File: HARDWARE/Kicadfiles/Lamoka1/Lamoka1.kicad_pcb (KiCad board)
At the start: 2 copper layers, 156.4 x 124.8 mm, 136 parts, among them IC1 INA240A2DR, J1 2606-1108/010-000, J2 2606-1352, J3 USB_C_Receptacle_USB2.0_14P, J4 470531000, J5 2604-1103, J6 Male-Header, J7 Male-Header, Q1 25V 60A N-Ch, Q2 30V 56A N-Ch, Q3 100V 150A N-Ch, Q4 100V 150A N-Ch, Q5 100V 150A N-Ch, Q6 100V 150A N-Ch, SW1 B3F-4055, U1 RP2354A, U10 ADS7128IRTER, U2 AMS1117-3.3, U3 74AHCT1G125, U4 LM5122MH/NOPB, U5 UCC27735DR, U6 UCC27735DR, U7 TPS62160DSGR, U8 TMP235A2DBZR, U9 TMP235A2DBZR, X1 ABM8-272-T3

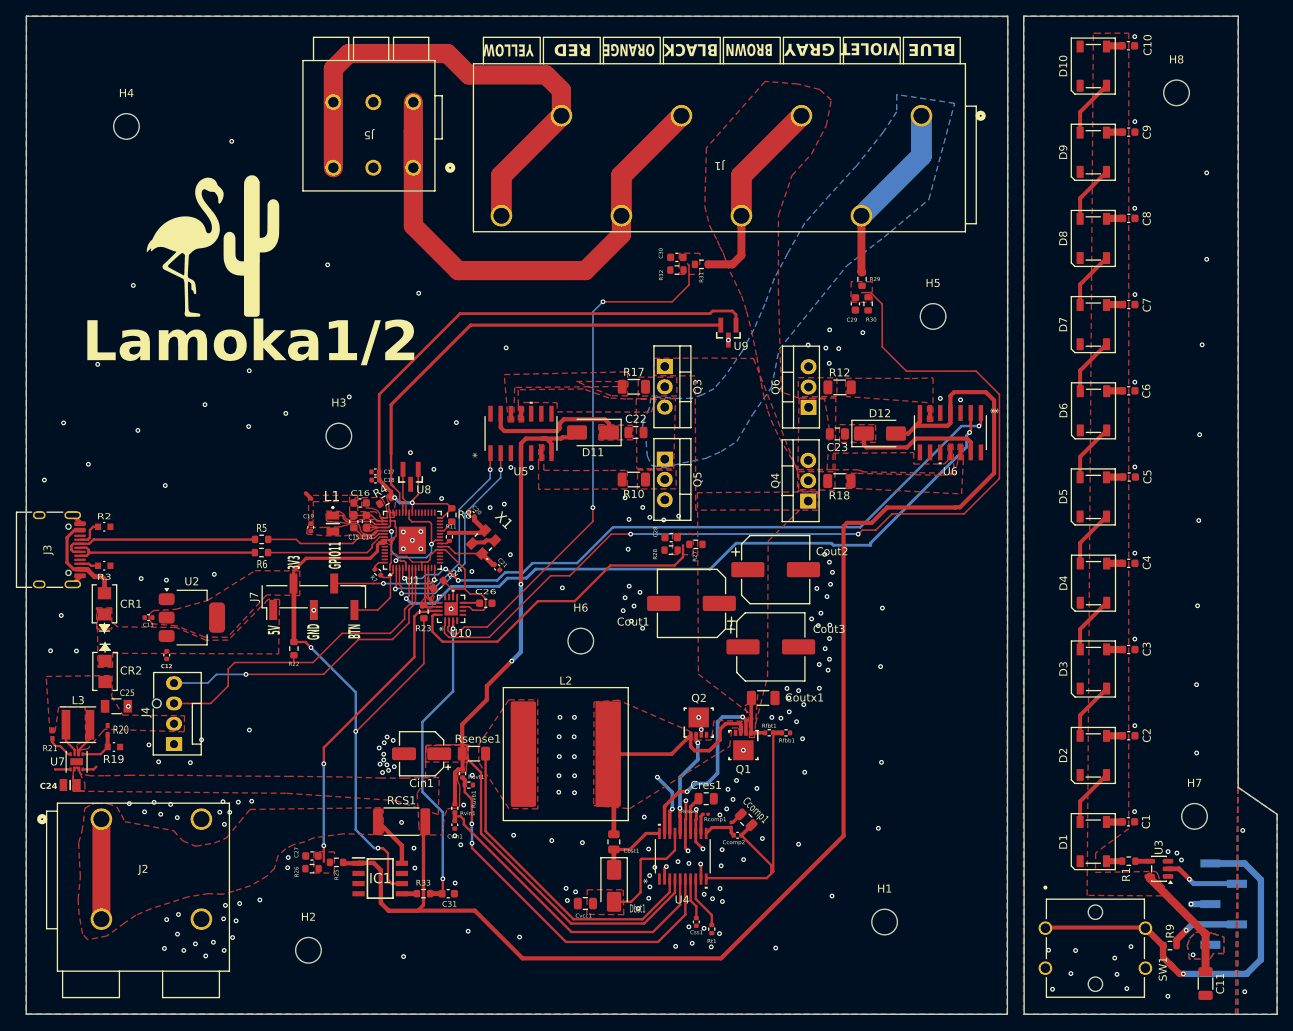
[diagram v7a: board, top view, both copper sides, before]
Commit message: Some more slight improvements, general. ADD picture to main readme, etc
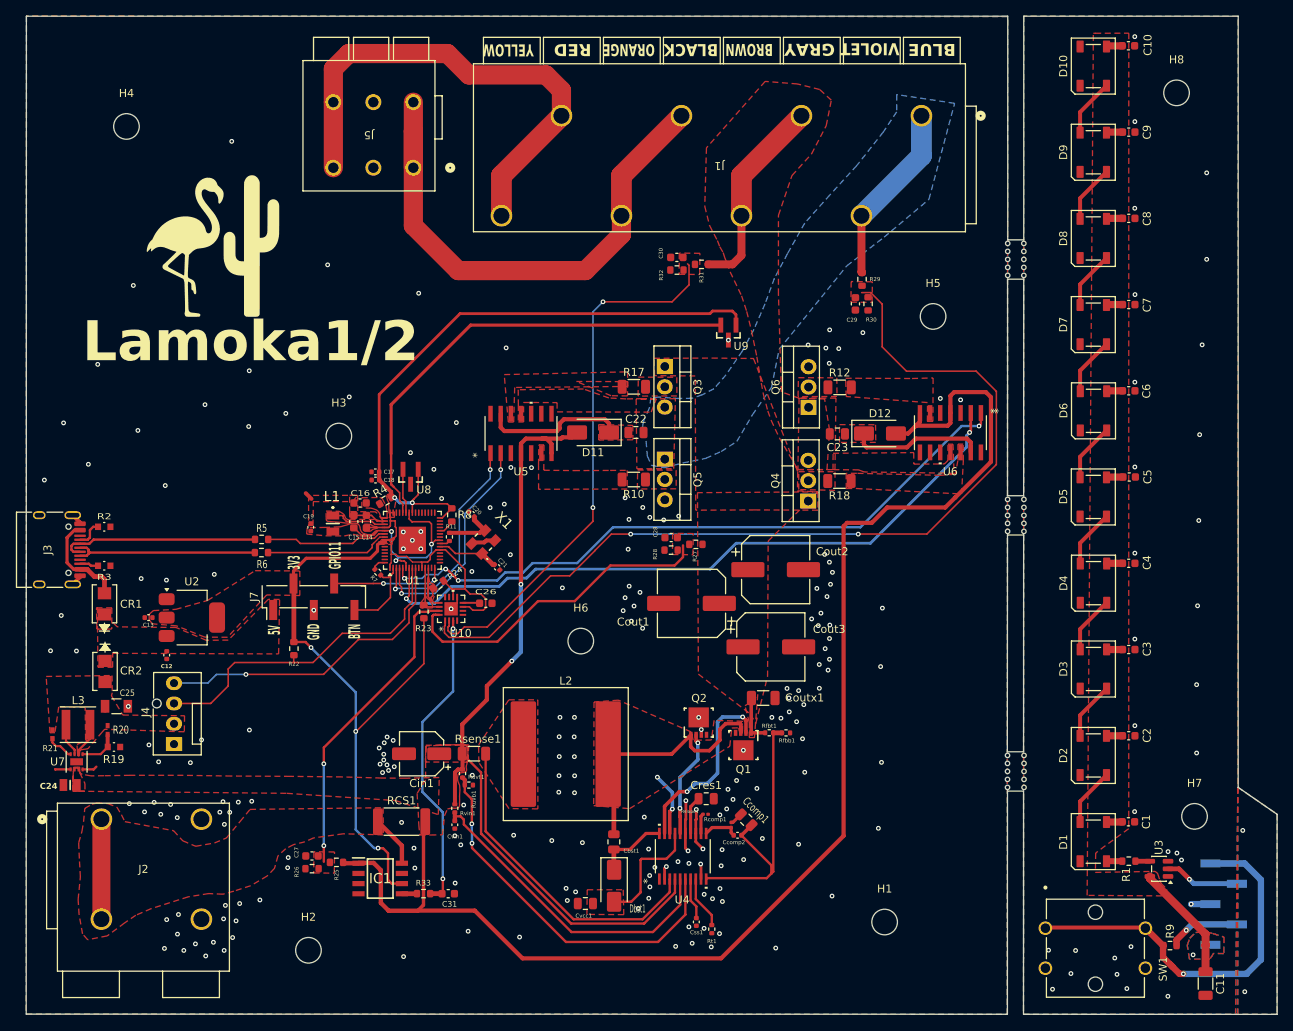
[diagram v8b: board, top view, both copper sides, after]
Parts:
- added MTB1: MouseBite-5x0.55, MouseBite-5x0.55, F.Cu at (179.5, 60.0)
- added MTB2: MouseBite-5x0.55, MouseBite-5x0.55, F.Cu at (179.5, 92.0)
- added MTB3: MouseBite-5x0.55, MouseBite-5x0.55, F.Cu at (179.5, 124.0)
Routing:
- net /Control-Section/AIN2: track 115.5 -> 114.0 mm
- net /Inversion-Section/CSP: track 278.9 -> 277.5 mm
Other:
- outline, holes or cut-outs redrawn
- board text added: "Danger! High Voltage."
- board text added: "PANEL 1x MAIN + 1x SUB - TAB-ROUTE 2mm - 3x TABS MTB1-3 - 0.55mm BITES - BREAK APART"
